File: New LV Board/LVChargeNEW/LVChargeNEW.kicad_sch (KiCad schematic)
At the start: 45 parts, among them Q1 CSD15380F3T, Q2 CSD15380F3T, Q3 CSD15380F3T, Q4 CSD15380F3T, U1 PQ25856QWRRVRQ1

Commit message: For real this time
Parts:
- added C_sys2, C_sys3, C_sys4, C_sys5, C_sys6, C_sys7, C_sys8, C_sys9: 100u, Capacitor_SMD:C_1210_3225Metric_Pad1.33x2.70mm_HandSolder, symbol Device:C
- added R18: 10k, Resistor_THT:R_Axial_DIN0204_L3.6mm_D1.6mm_P5.08mm_Horizontal, symbol Device:R
- C_sys1: value C -> 100u; footprint (none) -> Capacitor_SMD:C_1210_3225Metric_Pad1.33x2.70mm_HandSolder
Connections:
- net Batt+: now also C_sys2.2, C_sys3.2, C_sys4.2, C_sys5.2, C_sys6.2, C_sys7.2, C_sys8.2, C_sys9.2
- net GND: now also C_sys2.1, C_sys3.1, C_sys4.1, C_sys5.1, C_sys6.1, C_sys7.1, C_sys8.1, C_sys9.1, R18.2
- net Batt3: no longer names the net of R6.2, R9.1, U1.8 (TS)
- net Batt3: now also R18.1

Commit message: updated LVCharge
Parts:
- added J1: Conn_01x04_Socket, Connector_PinSocket_1.27mm:PinSocket_1x04_P1.27mm_Vertical, symbol Connector:Conn_01x04_Socket
- added J2: Conn_01x05_Socket, Connector_PinSocket_1.27mm:PinSocket_1x06_P1.27mm_Vertical, symbol Connector:Conn_01x05_Socket
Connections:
- net Batt+: now also J1.1 (Pin_1)
- net Buck Input: now also J1.4 (Pin_4)
- net CE: now also J2.2 (Pin_2)
- net GND: now also J1.2 (Pin_2), J1.3 (Pin_3), J2.1 (Pin_1)
- net INT: now also J2.3 (Pin_3)
- net SCL: now also J2.5 (Pin_5)
- net SDL: now also J2.4 (Pin_4)
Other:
- company: (none) -> Lafayette Motorsports
- title: (none) -> LV Charge Board
- moved on the sheet: C_sys2, C_sys3, C_sys4, C_sys5, C_sys6, C_sys7, C_sys8, C_sys9

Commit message: update lvcharge
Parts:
- R_bat_ac1, R_bat_sns1: footprint (none) -> LVChargeNEWLocalFootprints:RESC2012X80N
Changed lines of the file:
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@@
 			)
 		)
-		(property "Footprint" ""
+		(property "Footprint" "LVChargeNEWLocalFootprints:RESC2012X80N"
 			(at 318.77 46.228 90)
 			(effects
@@
 			)
 		)
-		(property "Footprint" ""
+		(property "Footprint" "LVChargeNEWLocalFootprints:RESC2012X80N"
 			(at 109.728 99.06 90)
 			(effects

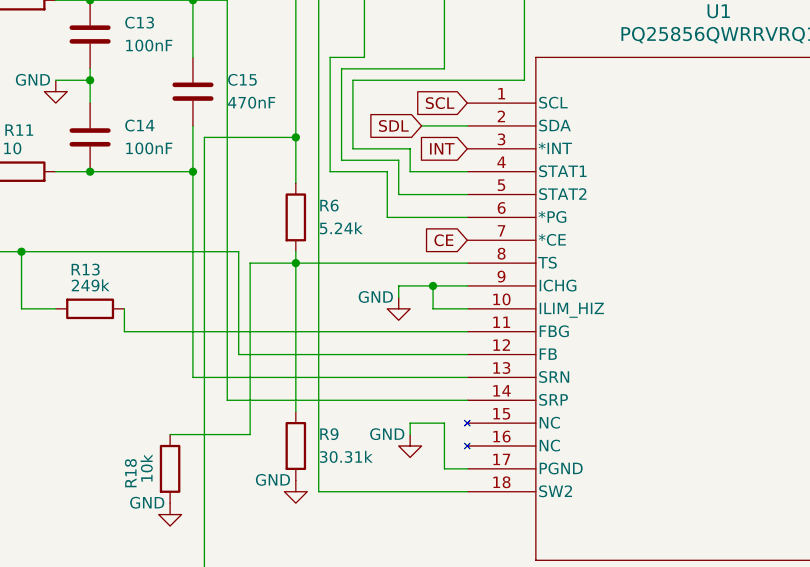
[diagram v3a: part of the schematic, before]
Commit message: add Ichg limit resistor
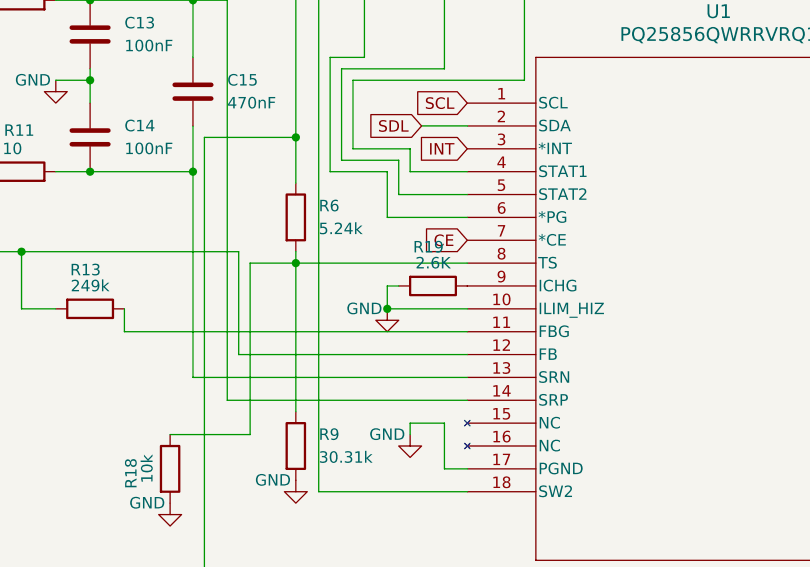
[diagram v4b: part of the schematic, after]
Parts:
- added R19: 2.6K, Resistor_THT:R_Axial_DIN0204_L3.6mm_D1.6mm_P5.08mm_Horizontal, symbol Device:R
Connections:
- net GND: now also R19.2; no longer U1.9 (ICHG)
- new net: R19.1, U1.9 (ICHG)
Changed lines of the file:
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@@
 	)
 	(junction
+		(at 163.83 124.46)
+		(diameter 0)
+		(color 0 0 0 0)
+	)
+	(junction
 		(at 306.07 44.45)
 		(diameter 0)
@@
 	)
 	(junction
-		(at 168.91 121.92)
-		(diameter 0)
-		(color 0 0 0 0)
-	)
-	(junction
 		(at 259.08 109.22)
 		(diameter 0)
@@
 	(wire
 		(pts
-			(xy 168.91 121.92) (xy 165.1 121.92)
+			(xy 163.83 124.46) (xy 172.72 124.46)
 		)
 		(stroke
@@
 	(wire
 		(pts
-			(xy 146.05 90.17) (xy 146.05 134.62)
+			(xy 163.83 121.92) (xy 163.83 124.46)
 		)
 		(stroke
@@
 	(wire
 		(pts
-			(xy 257.81 49.53) (xy 176.53 49.53)
+			(xy 146.05 90.17) (xy 146.05 134.62)
 		)
 		(stroke
@@
 	(wire
 		(pts
-			(xy 87.63 137.16) (xy 76.2 125.73)
+			(xy 257.81 49.53) (xy 176.53 49.53)
 		)
 		(stroke
@@
 	(wire
 		(pts
-			(xy 107.95 102.87) (xy 107.95 109.22)
+			(xy 87.63 137.16) (xy 76.2 125.73)
 		)
 		(stroke
@@
 	(wire
 		(pts
-			(xy 172.72 124.46) (xy 168.91 124.46)
+			(xy 107.95 102.87) (xy 107.95 109.22)
 		)
 		(stroke
@@
 	(wire
 		(pts
-			(xy 168.91 121.92) (xy 172.72 121.92)
-		)
-		(stroke
-			(width 0)
-			(type default)
-		)
-	)
-	(wire
-		(pts
 			(xy 306.07 54.61) (xy 306.07 57.15)
 		)
@@
 	(wire
 		(pts
-			(xy 168.91 124.46) (xy 168.91 121.92)
-		)
-		(stroke
-			(width 0)
-			(type default)
-		)
-	)
-	(wire
-		(pts
 			(xy 86.36 134.62) (xy 76.2 124.46)
 		)
@@
 	(wire
 		(pts
-			(xy 165.1 121.92) (xy 165.1 123.19)
-		)
-		(stroke
-			(width 0)
-			(type default)
-		)
-	)
-	(wire
-		(pts
 			(xy 243.84 147.32) (xy 243.84 152.4)
 		)
@@
 	(wire
 		(pts
+			(xy 163.83 121.92) (xy 165.1 121.92)
+		)
+		(stroke
+			(width 0)
+			(type default)
+		)
+	)
+	(wire
+		(pts
 			(xy 143.51 105.41) (xy 153.67 105.41)
 		)
@@
 	)
 	(symbol
+		(lib_id "Device:R")
+		(at 168.91 121.92 270)
+		(unit 1)
+		(exclude_from_sim no)
+		(in_bom yes)
+		(on_board yes)
+		(dnp no)
+		(property "Reference" "R19"
+			(at 168.402 117.602 90)
+			(effects
+				(font
+					(size 1.27 1.27)
+				)
+			)
+		)
+		(property "Value" "2.6K"
+			(at 168.91 119.38 90)
+			(effects
+				(font
+					(size 1.27 1.27)
+				)
+			)
+		)
+		(property "Footprint" "Resistor_THT:R_Axial_DIN0204_L3.6mm_D1.6mm_P5.08mm_Horizontal"
+			(at 168.91 120.142 90)
+			(effects
+				(font
+					(size 1.27 1.27)
+				)
+				(hide yes)
+			)
+		)
+		(property "Datasheet" "~"
+			(at 168.91 121.92 0)
+			(effects
+				(font
+					(size 1.27 1.27)
+				)
+				(hide yes)
+			)
+		)
+		(property "Description" "Resistor"
+			(at 168.91 121.92 0)
+			(effects
+				(font
+					(size 1.27 1.27)
+				)
+				(hide yes)
+			)
+		)
+		(pin "1"
+		)
+		(pin "2"
+		)
+		(instances
+			(project "LVChargeNEW"
+				(path "/59e99d5c-d319-4165-bae5-97831157ea3a"
+					(reference "R19")
+					(unit 1)
+				)
+			)
+		)
+	)
+	(symbol
 		(lib_id "Connector:Conn_01x04_Socket")
 		(at 100.33 134.62 0)
@@
 	(symbol
 		(lib_id "power:GND")
-		(at 165.1 123.19 0)
+		(at 163.83 124.46 0)
 		(unit 1)
 		(exclude_from_sim no)
@@
 		(dnp no)
 		(property "Reference" "#PWR015"
-			(at 165.1 129.54 0)
+			(at 163.83 130.81 0)
 			(effects
 				(font
@@
 		)
 		(property "Value" "GND"
-			(at 162.56 123.19 0)
+			(at 161.29 124.46 0)
 			(effects
 				(font
@@
 		)
 		(property "Footprint" ""
-			(at 165.1 123.19 0)
+			(at 163.83 124.46 0)
 			(effects
 				(font
@@
 		)
 		(property "Datasheet" ""
-			(at 165.1 123.19 0)
+			(at 163.83 124.46 0)
 			(effects
 				(font
@@
 		)
 		(property "Description" "Power symbol creates a global label with name \"GND\" , ground"
-			(at 165.1 123.19 0)
+			(at 163.83 124.46 0)
 			(effects
 				(font

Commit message: up
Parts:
- added R20: 249k, Resistor_THT:R_Axial_DIN0204_L3.6mm_D1.6mm_P5.08mm_Horizontal, symbol Device:R
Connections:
- net GND: now also R20.2; no longer C_sys1.1, C_sys2.1, C_sys3.1, C_sys4.1, C_sys5.1, C_sys6.1, C_sys7.1, C_sys8.1, C_sys9.1
- new net: C_sys1.1, C_sys2.1, C_sys3.1, C_sys4.1, C_sys5.1, C_sys6.1, C_sys7.1, C_sys8.1, C_sys9.1, R20.1
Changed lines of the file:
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@@
-	(wire
-		(pts
-			(xy 73.66 97.79) (xy 80.01 97.79)
-		)
-		(stroke
-			(width 0)
-			(type default)
-		)
-	)
 	(wire
 		(pts
@@
 	(wire
 		(pts
+			(xy 80.01 93.98) (xy 80.01 101.6)
+		)
+		(stroke
+			(width 0)
+			(type default)
+		)
+	)
+	(wire
+		(pts
 			(xy 228.6 134.62) (xy 236.22 134.62)
 		)
@@
 		(pts
 			(xy 232.41 44.45) (xy 232.41 58.42)
-		)
-		(stroke
-			(width 0)
-			(type default)
-		)
-	)
-	(wire
-		(pts
-			(xy 80.01 97.79) (xy 80.01 101.6)
 		)
 		(stroke
@@
 	)
 	(symbol
+		(lib_id "Device:R")
+		(at 76.2 93.98 270)
+		(unit 1)
+		(exclude_from_sim no)
+		(in_bom yes)
+		(on_board yes)
+		(dnp no)
+		(fields_autoplaced yes)
+		(property "Reference" "R20"
+			(at 76.2 87.63 90)
+			(effects
+				(font
+					(size 1.27 1.27)
+				)
+			)
+		)
+		(property "Value" "249k"
+			(at 76.2 90.17 90)
+			(effects
+				(font
+					(size 1.27 1.27)
+				)
+			)
+		)
+		(property "Footprint" "Resistor_THT:R_Axial_DIN0204_L3.6mm_D1.6mm_P5.08mm_Horizontal"
+			(at 76.2 92.202 90)
+			(effects
+				(font
+					(size 1.27 1.27)
+				)
+				(hide yes)
+			)
+		)
+		(property "Datasheet" "~"
+			(at 76.2 93.98 0)
+			(effects
+				(font
+					(size 1.27 1.27)
+				)
+				(hide yes)
+			)
+		)
+		(property "Description" "Resistor"
+			(at 76.2 93.98 0)
+			(effects
+				(font
+					(size 1.27 1.27)
+				)
+				(hide yes)
+			)
+		)
+		(pin "1"
+		)
+		(pin "2"
+		)
+		(instances
+			(project "LVChargeNEW"
+				(path "/59e99d5c-d319-4165-bae5-97831157ea3a"
+					(reference "R20")
+					(unit 1)
+				)
+			)
+		)
+	)
+	(symbol
 		(lib_id "Device:C")
 		(at 334.01 60.96 0)
@@
 	(symbol
 		(lib_id "power:GND")
-		(at 73.66 97.79 0)
+		(at 72.39 93.98 0)
 		(unit 1)
 		(exclude_from_sim no)
@@
 		(dnp no)
 		(property "Reference" "#PWR013"
-			(at 73.66 104.14 0)
+			(at 72.39 100.33 0)
 			(effects
 				(font
@@
 		)
 		(property "Value" "GND"
-			(at 71.12 97.79 0)
+			(at 69.85 93.98 0)
 			(effects
 				(font
@@
 		)
 		(property "Footprint" ""
-			(at 73.66 97.79 0)
+			(at 72.39 93.98 0)
 			(effects
 				(font
@@
 		)
 		(property "Datasheet" ""
-			(at 73.66 97.79 0)
+			(at 72.39 93.98 0)
 			(effects
 				(font
@@
 		)
 		(property "Description" "Power symbol creates a global label with name \"GND\" , ground"
-			(at 73.66 97.79 0)
-			(effects
-				(font
+			(at 72.39 93.98 0)
+			(effects
+				(font

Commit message: up!
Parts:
- removed J1: Conn_01x04_Socket, Connector_PinSocket_1.27mm:PinSocket_1x04_P1.27mm_Vertical, symbol Connector:Conn_01x04_Socket
- added J1, J2: Conn_01x02, symbol Connector_Generic:Conn_01x02
- renumbered J2 to J3
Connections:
- net Batt+: now also J1.1 (Pin_1)
- net Buck Input: now also J2.2 (Pin_2)
- net GND: now also J1.2 (Pin_2), J2.1 (Pin_1)
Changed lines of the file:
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@@
 	(wire
 		(pts
+			(xy 101.6 137.16) (xy 104.14 139.7)
+		)
+		(stroke
+			(width 0)
+			(type default)
+		)
+	)
+	(wire
+		(pts
 			(xy 243.84 147.32) (xy 243.84 152.4)
 		)
@@
 	(wire
 		(pts
-			(xy 95.25 134.62) (xy 86.36 134.62)
+			(xy 86.36 134.62) (xy 104.14 134.62)
 		)
 		(stroke
@@
 	(wire
 		(pts
-			(xy 95.25 137.16) (xy 87.63 137.16)
+			(xy 87.63 137.16) (xy 101.6 137.16)
 		)
 		(stroke
@@
 	(wire
 		(pts
+			(xy 101.6 139.7) (xy 104.14 142.24)
+		)
+		(stroke
+			(width 0)
+			(type default)
+		)
+	)
+	(wire
+		(pts
 			(xy 179.07 85.09) (xy 179.07 99.06)
 		)
@@
 	(wire
 		(pts
+			(xy 95.25 132.08) (xy 104.14 132.08)
+		)
+		(stroke
+			(width 0)
+			(type default)
+		)
+	)
+	(wire
+		(pts
 			(xy 163.83 114.3) (xy 163.83 109.22)
 		)
@@
 	(wire
 		(pts
-			(xy 85.09 139.7) (xy 95.25 139.7)
+			(xy 85.09 139.7) (xy 101.6 139.7)
 		)
 		(stroke
@@
 		(on_board yes)
 		(dnp no)
-		(property "Reference" "J2"
+		(property "Reference" "J3"
 			(at 93.218 160.02 0)
 			(effects
@@
 			(project ""
 				(path "/59e99d5c-d319-4165-bae5-97831157ea3a"
-					(reference "J2")
+					(reference "J3")
 					(unit 1)
 				)
@@
 	)
 	(symbol
-		(lib_id "Connector:Conn_01x04_Socket")
-		(at 100.33 134.62 0)
-		(unit 1)
-		(exclude_from_sim no)
-		(in_bom yes)
-		(on_board yes)
-		(dnp no)
-		(property "Reference" "J1"
-			(at 96.52 144.78 0)
-			(effects
-				(font
-					(size 1.27 1.27)
-				)
-				(justify left)
-			)
-		)
-		(property "Value" "Conn_01x04_Socket"
-			(at 96.266 142.494 0)
-			(effects
-				(font
-					(size 1.27 1.27)
-				)
-				(justify left)
-			)
-		)
-		(property "Footprint" "Connector_PinSocket_1.27mm:PinSocket_1x04_P1.27mm_Vertical"
-			(at 100.33 134.62 0)
-			(effects
-				(font
-					(size 1.27 1.27)
-				)
-				(hide yes)
-			)
-		)
-		(property "Datasheet" "~"
-			(at 100.33 134.62 0)
-			(effects
-				(font
-					(size 1.27 1.27)
-				)
-				(hide yes)
-			)
-		)
-		(property "Description" "Generic connector, single row, 01x04, script generated"
-			(at 100.33 134.62 0)
-			(effects
-				(font
-					(size 1.27 1.27)
-				)
-				(hide yes)
-			)
-		)
-		(pin "3"
-		)
-		(pin "4"
-		)
-		(pin "2"
-		)
-		(pin "1"
-		)
-		(instances
-			(project ""
-				(path "/59e99d5c-d319-4165-bae5-97831157ea3a"
-					(reference "J1")
-					(unit 1)
-				)
-			)
-		)
-	)
-	(symbol
 		(lib_id "power:GND")
 		(at 139.7 146.05 0)
@@
 	)
 	(symbol
+		(lib_id "Connector_Generic:Conn_01x02")
+		(at 109.22 132.08 0)
+		(unit 1)
+		(exclude_from_sim no)
+		(in_bom yes)
+		(on_board yes)
+		(dnp no)
+		(fields_autoplaced yes)
+		(property "Reference" "J1"
+			(at 111.76 132.0799 0)
+			(effects
+				(font
+					(size 1.27 1.27)
+				)
+				(justify left)
+			)
+		)
+		(property "Value" "Conn_01x02"
+			(at 111.76 134.6199 0)
+			(effects
+				(font
+					(size 1.27 1.27)
+				)
+				(justify left)
+			)
+		)
+		(property "Footprint" ""
+			(at 109.22 132.08 0)
+			(effects
+				(font
+					(size 1.27 1.27)
+				)
+				(hide yes)
+			)
+		)
+		(property "Datasheet" "~"
+			(at 109.22 132.08 0)
+			(effects
+				(font
+					(size 1.27 1.27)
+				)
+				(hide yes)
+			)
+		)
+		(property "Description" "Generic connector, single row, 01x02, script generated (kicad-library-utils/schlib/autogen/connector/)"
+			(at 109.22 132.08 0)
+			(effects
+				(font
+					(size 1.27 1.27)
+				)
+				(hide yes)
+			)
+		)
+		(pin "2"
+		)
+		(pin "1"
+		)
+		(instances
+			(project ""
+				(path "/59e99d5c-d319-4165-bae5-97831157ea3a"
+					(reference "J1")
+					(unit 1)
+				)
+			)
+		)
+	)
+	(symbol
 		(lib_id "Device:R")
 		(at 179.07 81.28 0)
@@
 					(unit 1)
 				)
+			)
+		)
+	)
+	(symbol
+		(lib_id "Connector_Generic:Conn_01x02")
+		(at 109.22 139.7 0)
+		(unit 1)
+		(exclude_from_sim no)
+		(in_bom yes)
+		(on_board yes)
+		(dnp no)
+		(fields_autoplaced yes)
+		(property "Reference" "J2"
+			(at 111.76 139.6999 0)
+			(effects
+				(font
+					(size 1.27 1.27)
+				)
+				(justify left)
+			)
+		)
+		(property "Value" "Conn_01x02"
+			(at 111.76 142.2399 0)
+			(effects
+				(font
+					(size 1.27 1.27)
+				)
+				(justify left)
+			)
+		)
+		(property "Footprint" ""
+			(at 109.22 139.7 0)
+			(effects
+				(font
+					(size 1.27 1.27)
+				)
+				(hide yes)
+			)
+		)
+		(property "Datasheet" "~"
+			(at 109.22 139.7 0)
+			(effects
+				(font
+					(size 1.27 1.27)
+				)
+				(hide yes)
+			)
+		)
+		(property "Description" "Generic connector, single row, 01x02, script generated (kicad-library-utils/schlib/autogen/connector/)"
+			(at 109.22 139.7 0)
+			(effects
+				(font
+					(size 1.27 1.27)
+				)
+				(hide yes)
+			)
+		)
+		(pin "2"
+		)
+		(pin "1"
+		)
+		(instances
+			(project "LVChargeNEW"
+				(path "/59e99d5c-d319-4165-bae5-97831157ea3a"
+					(reference "J2")
+					(unit 1)
+				)

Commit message: Changing names of folders good luck Jack!!!
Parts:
- added J4: 691137710002, motorsports:691137710002, symbol 691137710002:691137710002
- added K1: ALF1PF12, motorsports:RELAY_ALF1PF12, symbol ALF1PF12:ALF1PF12
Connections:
- new net: J4.1, K1.1, K1.3
- new net: J4.2, K1.4
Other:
- note added: "VBATT"
- note added: "VCU MPR"
- note added: "VCU Main Power Relay"
- note added: "VCU VBATT"

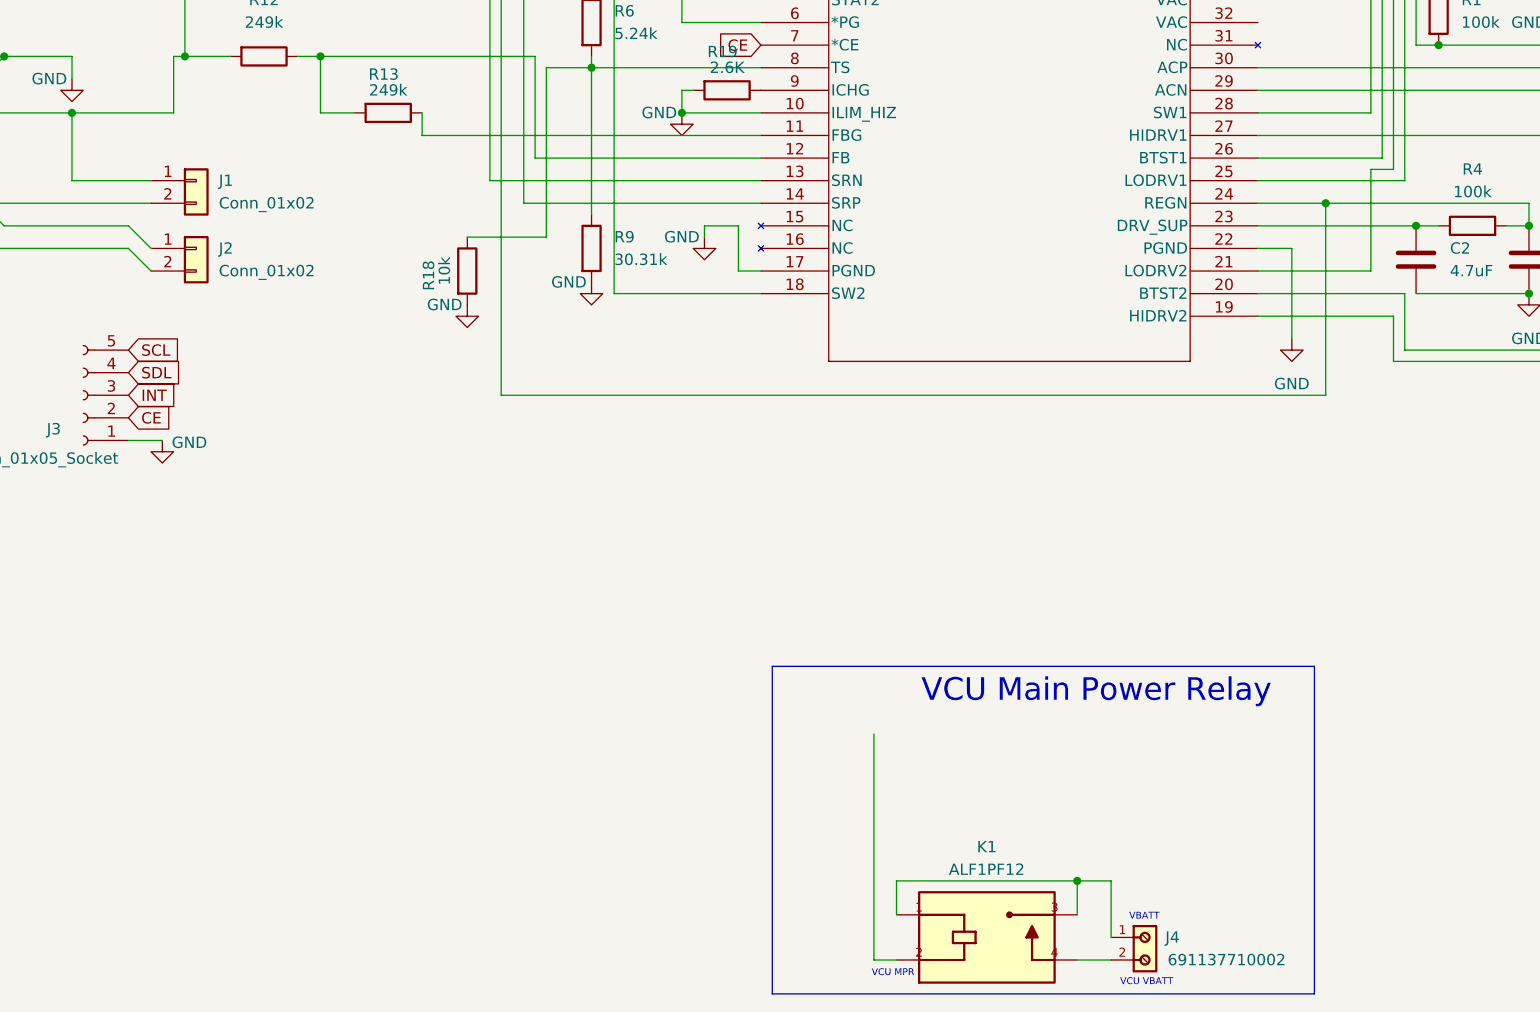
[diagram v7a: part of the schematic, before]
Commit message: LV Charge changes, traces changes
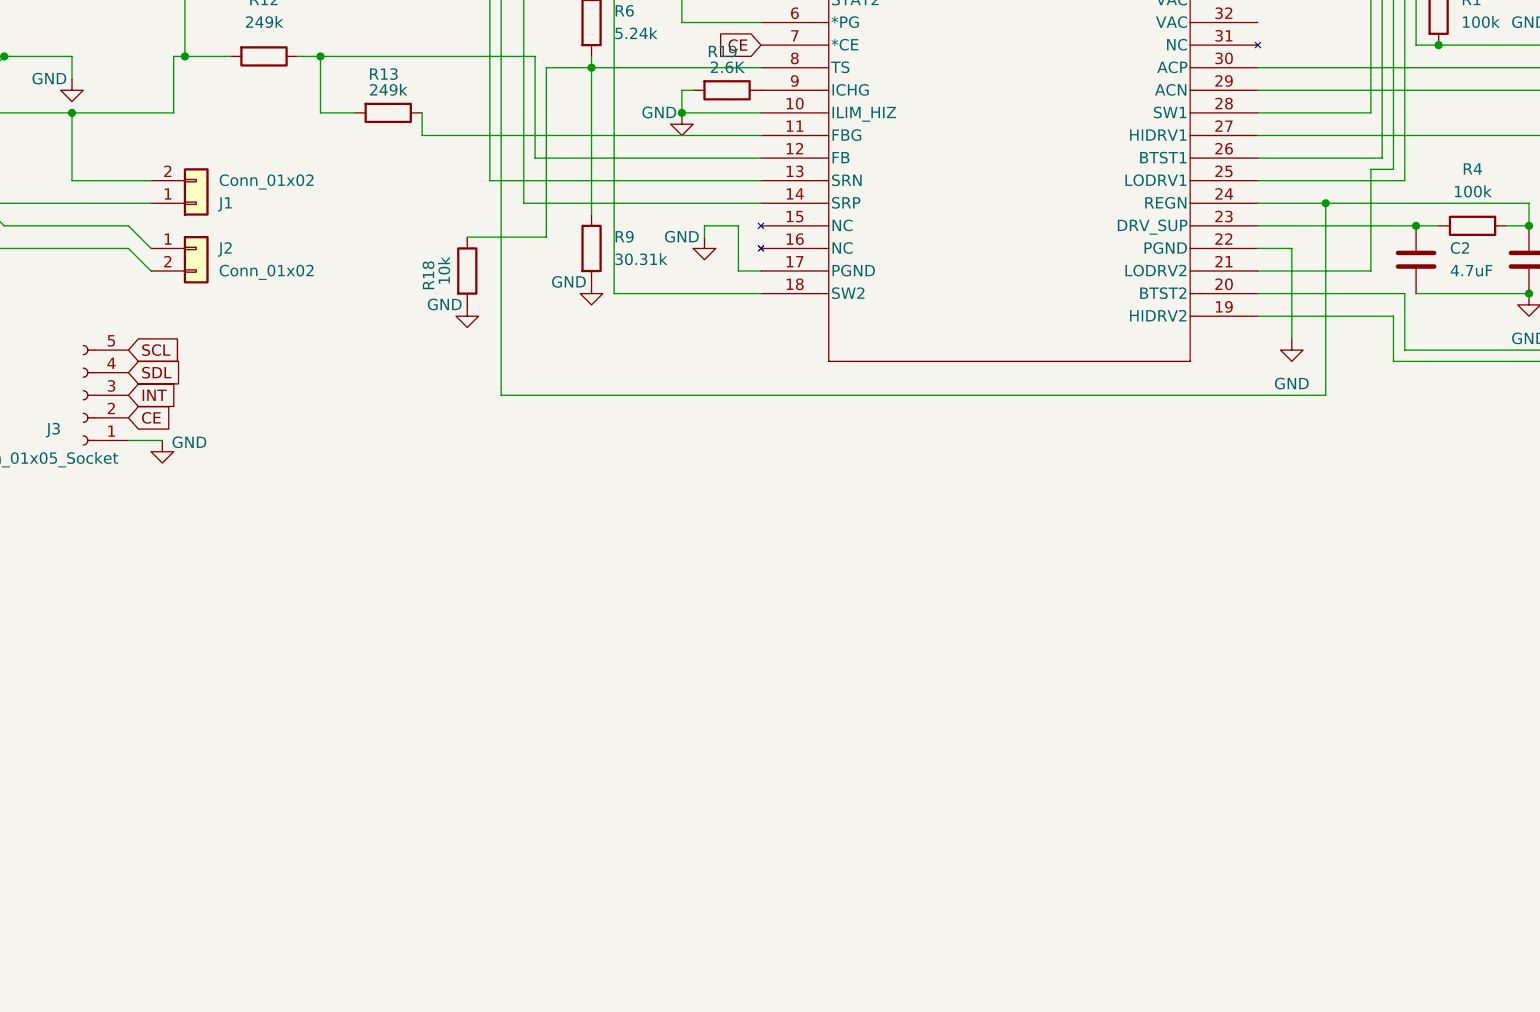
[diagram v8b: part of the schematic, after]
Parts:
- removed J4: 691137710002, motorsports:691137710002, symbol 691137710002:691137710002
- removed K1: ALF1PF12, motorsports:RELAY_ALF1PF12, symbol ALF1PF12:ALF1PF12
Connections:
- net Batt+: now also J1.2 (Pin_2); no longer J1.1 (Pin_1)
- net GND: now also J1.1 (Pin_1); no longer J1.2 (Pin_2)
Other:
- note removed: "VBATT"
- note removed: "VCU MPR"
- note removed: "VCU Main Power Relay"
- note removed: "VCU VBATT"
